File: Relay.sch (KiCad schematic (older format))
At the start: 11 parts

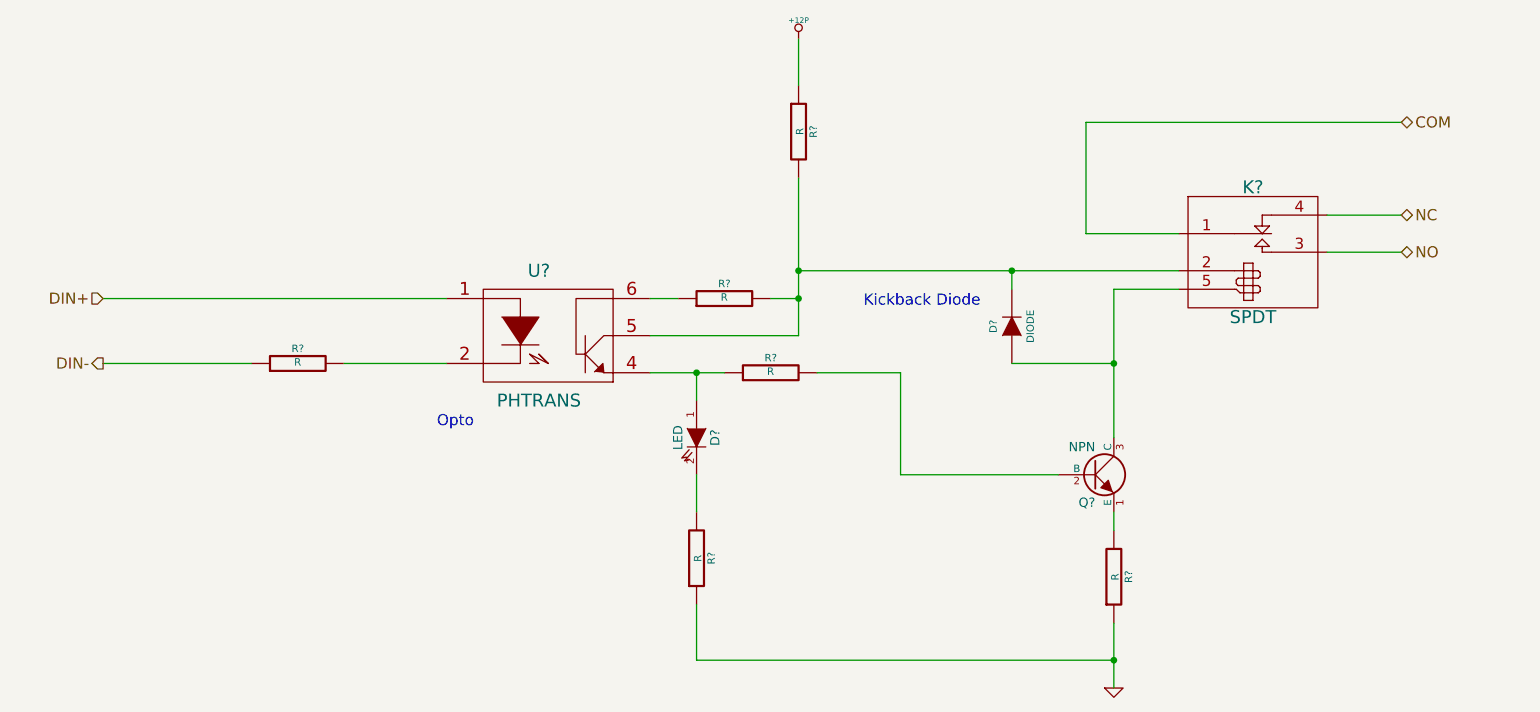
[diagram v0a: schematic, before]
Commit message: Changes up to and including Arduino module
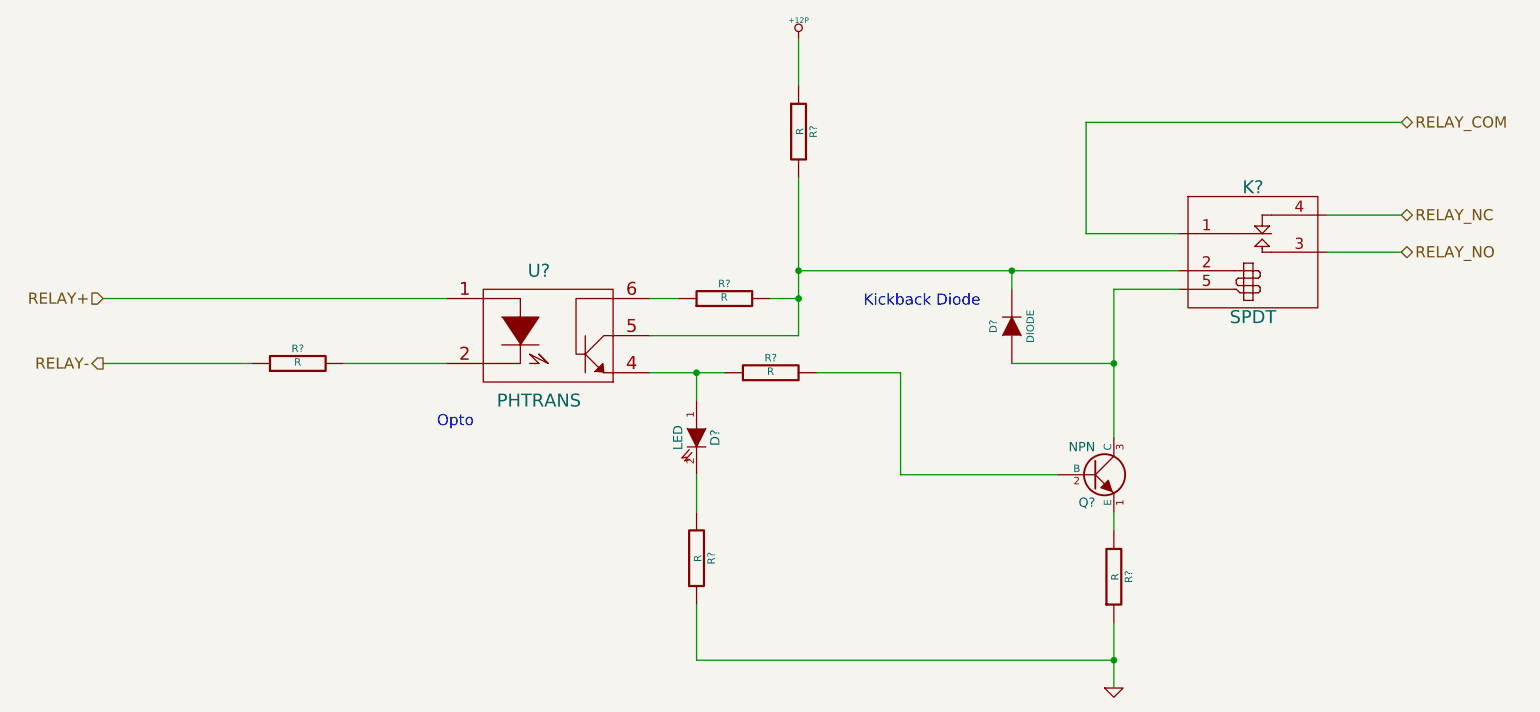
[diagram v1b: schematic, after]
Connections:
- net COM renamed RELAY_COM
- net DIN+ renamed RELAY+
- net DIN- renamed RELAY-
- net NC renamed RELAY_NC
- net NO renamed RELAY_NO
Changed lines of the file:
@@
 LIBS:valves
 LIBS:BencyBuddy
+LIBS:arduino_shieldsNCL
 LIBS:BenchBuddy-cache
 EELAYER 27 0
@@
 Sheet 3 9
 Title ""
-Date "9 feb 2014"
+Date "12 feb 2014"
 Rev ""
 Comp ""
@@
 $EndDescr
 Text HLabel 2400 2450 0    60   Input ~ 0
-DIN+
+RELAY+
 Text HLabel 2400 2800 0    60   Output ~ 0
-DIN-
+RELAY-
 Text HLabel 9400 2000 2    60   BiDi ~ 0
-NC
+RELAY_NC
 Text HLabel 9400 2200 2    60   BiDi ~ 0
-NO
+RELAY_NO
 $Comp
 L PHTRANS U?
@@
 $EndComp
 Text HLabel 9400 1500 2    60   BiDi ~ 0
-COM
+RELAY_COM
 Wire Wire Line
 	7700 2100 8200 2100
